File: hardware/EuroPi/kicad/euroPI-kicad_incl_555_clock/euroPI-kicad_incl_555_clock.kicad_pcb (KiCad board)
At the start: 2 copper layers, 121.9 x 128.5 mm, 108 parts, among them J1 Output 1 Jack, J10 Eurorack Power 2x8 16p, J11 Conn_01x13_Socket, J12 OLED 64x128, J13 USB_B_Micro, J14 Conn_01x03_Pin, J15 Conn_01x04_Pin, J16 Conn_02x04_Top_Bottom, J17 Conn_01x13_Pin, J18 Conn_01x04_Pin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

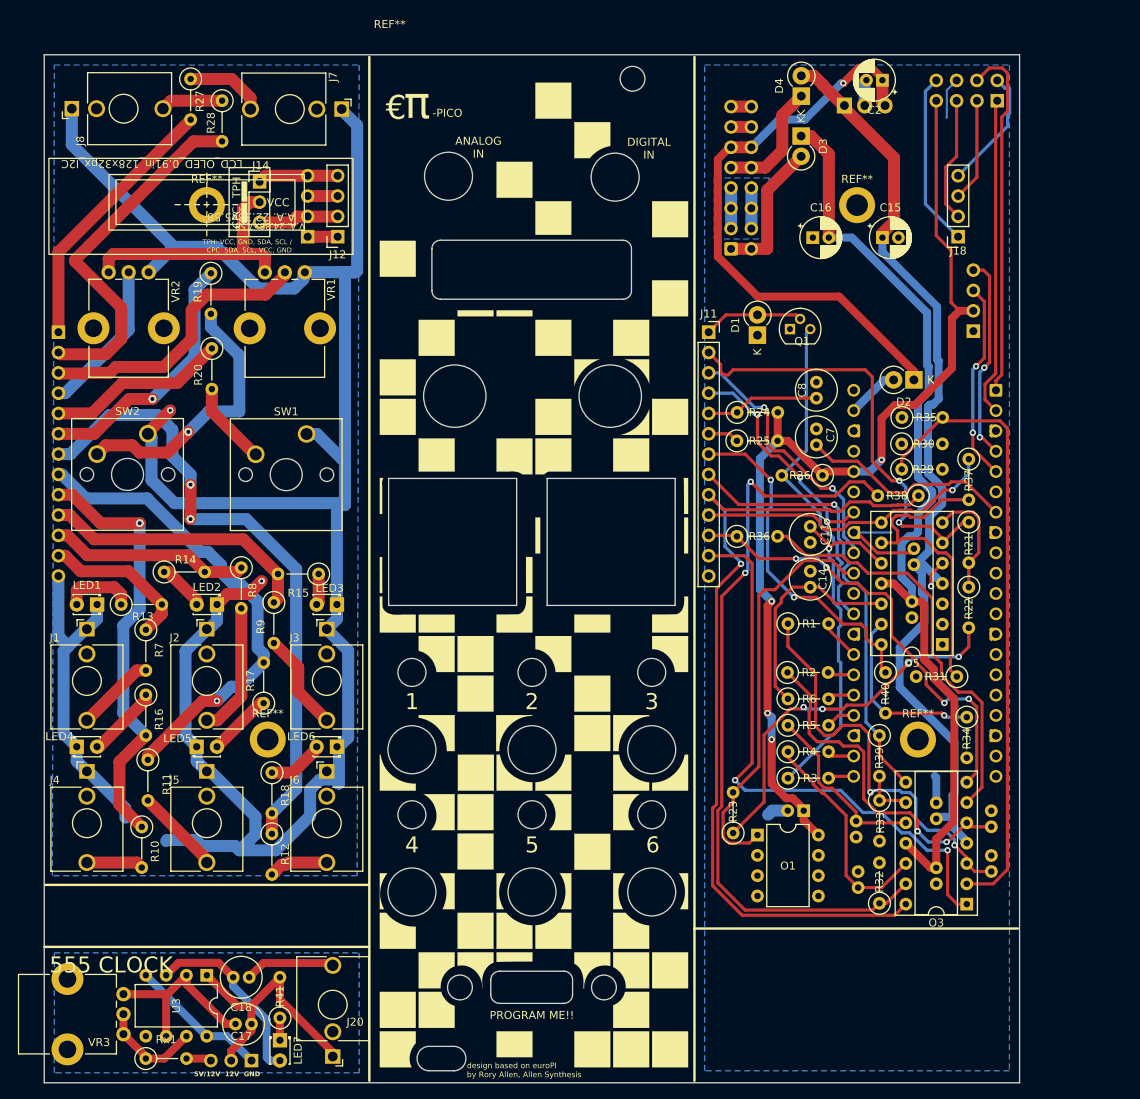
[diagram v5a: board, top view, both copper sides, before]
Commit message: incl standoffs to GND removed GND pin on headers
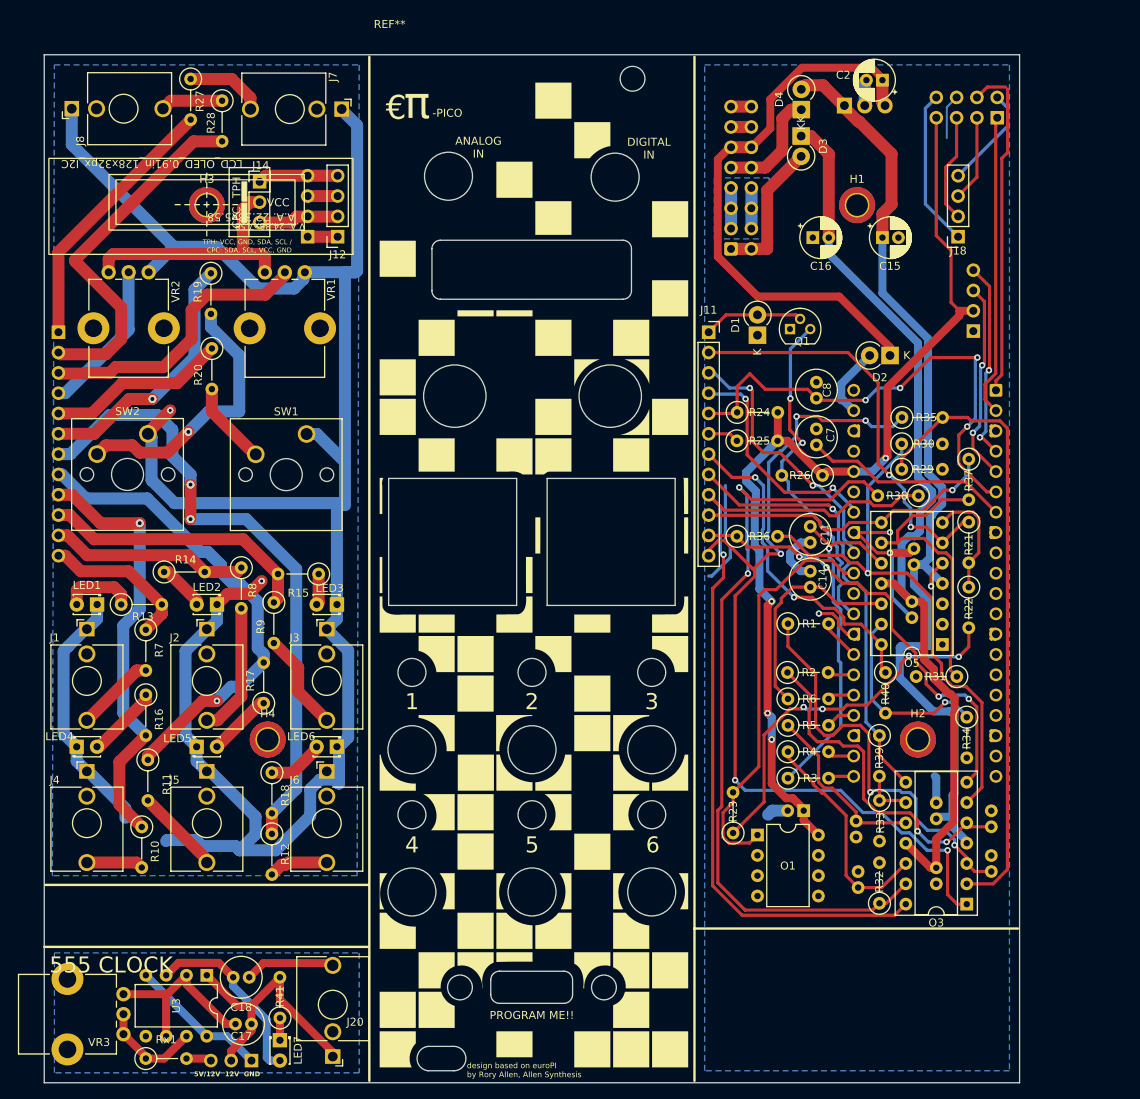
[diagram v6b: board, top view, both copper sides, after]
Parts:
- removed the REF** at (109.2, 111.0)
- removed the REF** at (101.6, 44.2)
- removed the REF** at (182.9, 44.2)
- removed the REF** at (190.5, 111.0)
- added H1: MountingHole_Pad, MountingHole:MountingHole_2.7mm_M2.5_ISO14580_Pad_TopBottom, F.Cu at (182.9, 44.2)
- added H2: MountingHole_Pad, MountingHole:MountingHole_2.7mm_M2.5_ISO14580_Pad_TopBottom, F.Cu at (190.5, 111.0)
- added H3: MountingHole_Pad, MountingHole:MountingHole_2.7mm_M2.5_ISO14580_Pad_TopBottom, F.Cu at (101.6, 44.2)
- added H4: MountingHole_Pad, MountingHole:MountingHole_2.7mm_M2.5_ISO14580_Pad_TopBottom, F.Cu at (109.2, 111.0)
- J11: value Conn_01x13_Socket -> Conn_01x12_Socket; footprint Connector_PinSocket_2.54mm:PinSocket_1x13_P2.54mm_Vertical -> Connector_PinSocket_2.54mm:PinSocket_1x12_P2.54mm_Vertical
- J17: value Conn_01x13_Pin -> Conn_01x12_Pin; footprint Connector_PinSocket_2.54mm:PinSocket_1x13_P2.54mm_Vertical -> Connector_PinHeader_2.54mm:PinHeader_1x12_P2.54mm_Vertical
- moved D2 4.27 mm to (187.0, 63.0)
- moved J16 2.12 mm to (200.4, 33.3)
- moved D4 1.69 mm to (175.9, 32.3)
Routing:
- net CS1: track 36.8 -> 84.0 mm, vias 0 -> 4
- net CJ1: track 91.9 -> 131.6 mm, vias 2 -> 5
- net I2C_GND: track 373.3 -> 399.3 mm, vias 3 -> 6
- net Net-(O3B--): track 52.4 -> 70.4 mm, vias 0 -> 1
- net CJA: track 100.3 -> 97.2 mm
- net TPH VCC / CPC SDA: track 25.7 -> 22.9 mm
- net ~: track 138.1 -> 140.9 mm
- net -12V: track 117.9 -> 115.3 mm
- net GP0: track 45.0 -> 42.4 mm
- net Net-(D2-K): track 6.58 -> 9.16 mm
- net +5V: track 76.4 -> 74.2 mm, vias 1 -> 0
- net TPH GND / CPC SCL: track 16.6 -> 14.4 mm
- net TPH SDA / CPC VCC: track 25.7 -> 23.6 mm
- net TPH SCL / CPC GND: track 25.5 -> 23.3 mm
- net GP1: track 39.9 -> 37.8 mm
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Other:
- board text added: "I2C"

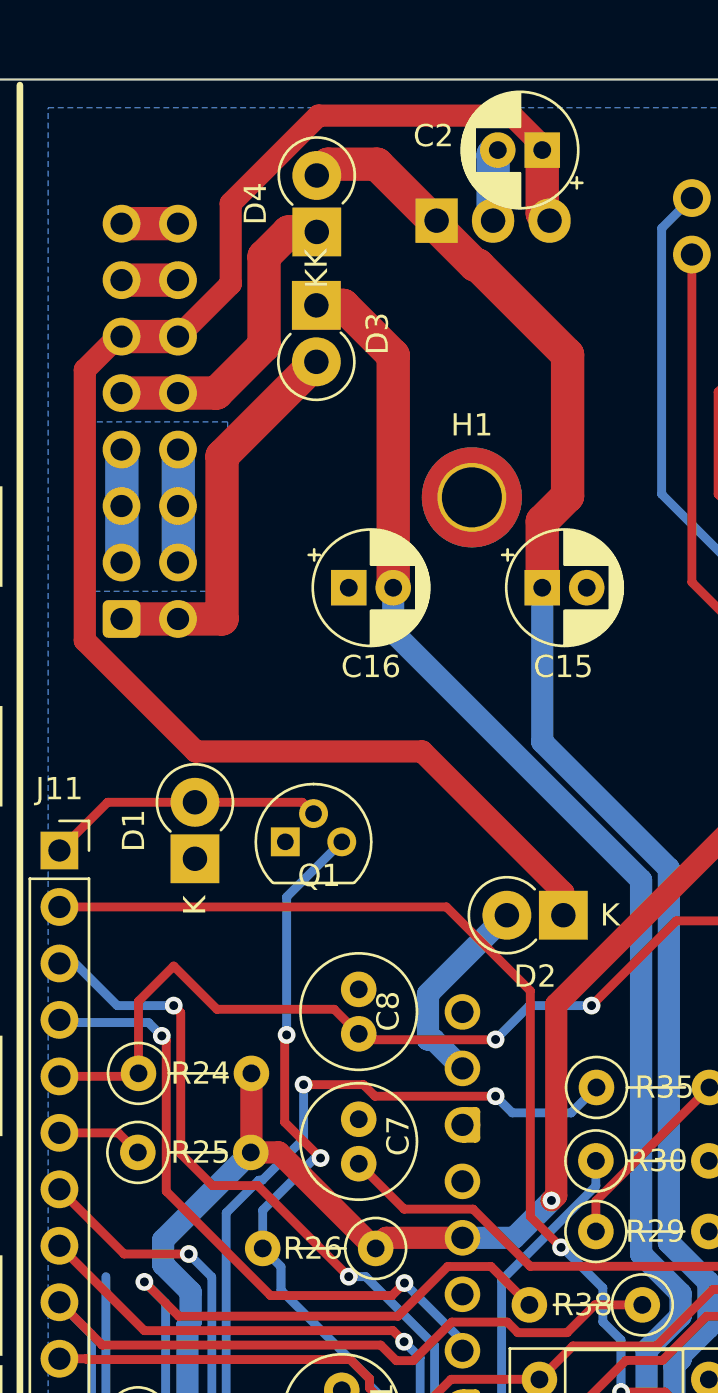
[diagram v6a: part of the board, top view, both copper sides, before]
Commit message: small fixes added missed net and text around eurorack conn
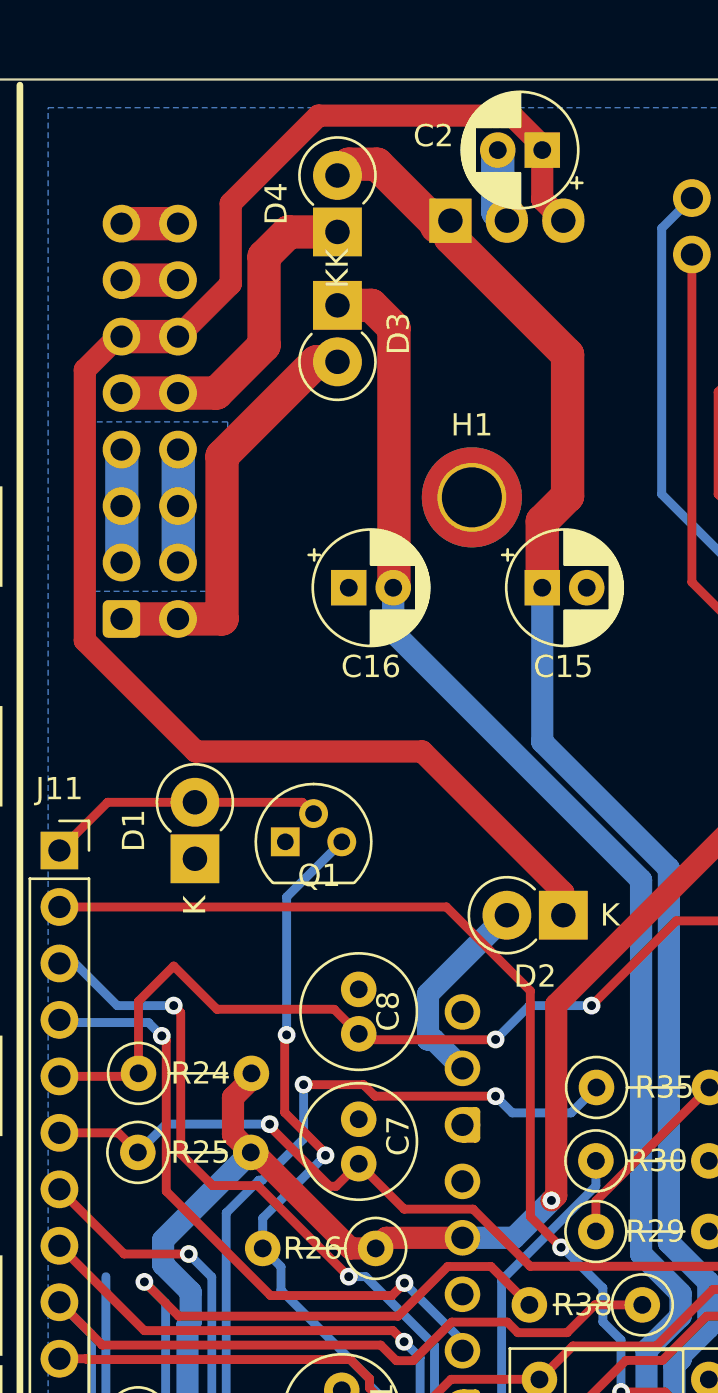
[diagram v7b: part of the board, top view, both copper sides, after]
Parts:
- moved D3 0.95 mm to (176.8, 35.6)
- moved D4 0.93 mm to (176.8, 32.3)
- moved U1 0.62 mm to (181.9, 31.8)
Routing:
- net CS2: track 62.1 -> 74.2 mm, vias 1 -> 2
- net ~: track 140.9 -> 139.8 mm
- net Net-(D3-K): track 17.9 -> 18.8 mm
- net Net-(D4-A): track 14.1 -> 15.0 mm
- net I2C_VCC: track 156.1 -> 156.8 mm
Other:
- board text added: "Gate CV +5V --- +12V GND GND GND -12V"

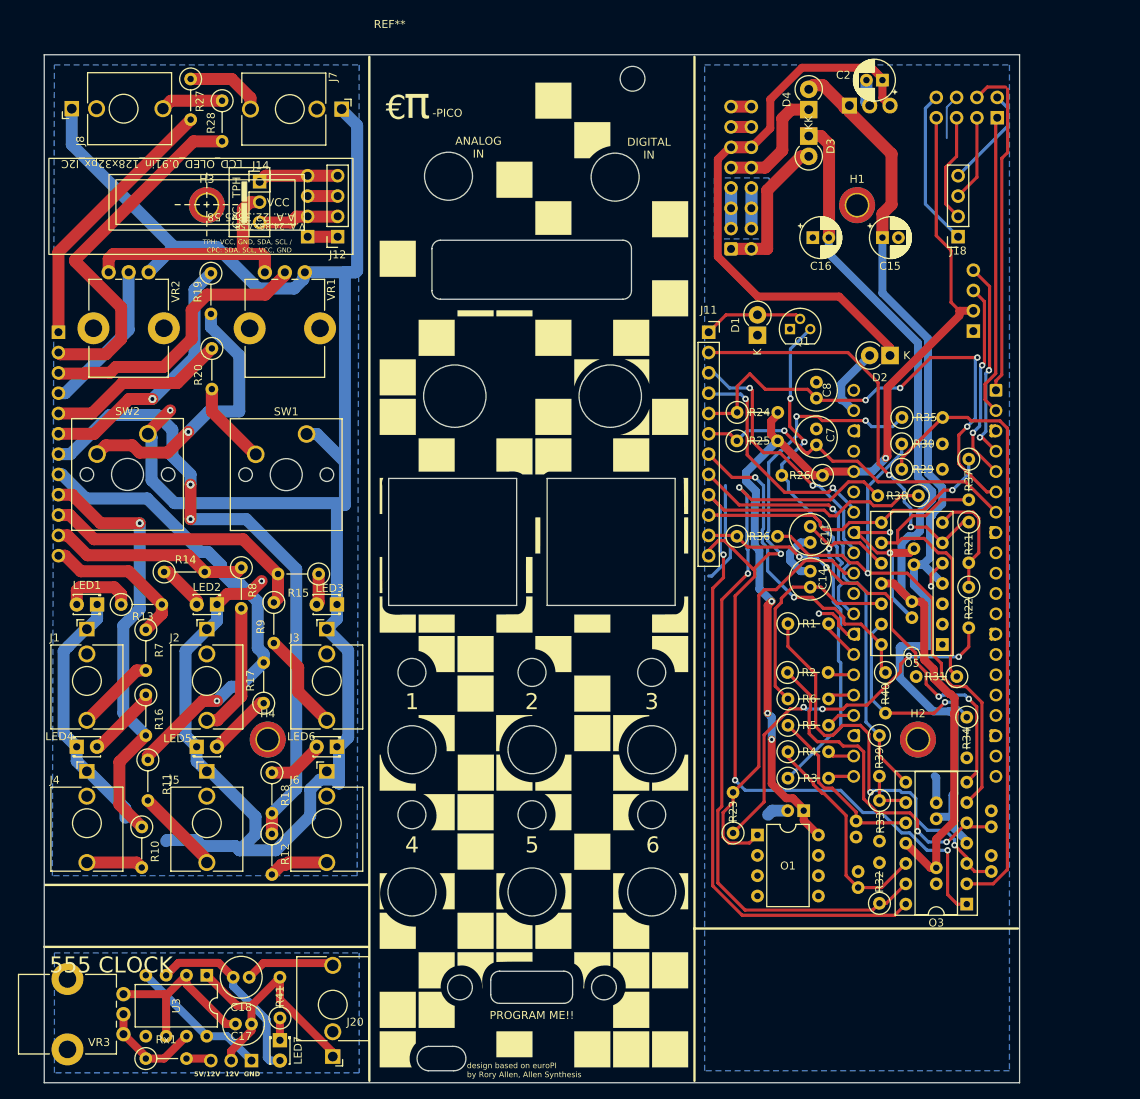
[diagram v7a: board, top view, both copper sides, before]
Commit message: misc improvements THT fixed grounds and misc clean up issue likely still wtih usb output SMT redid caps to be near to necessary fixed GND and misc things to make it easier to hand solder
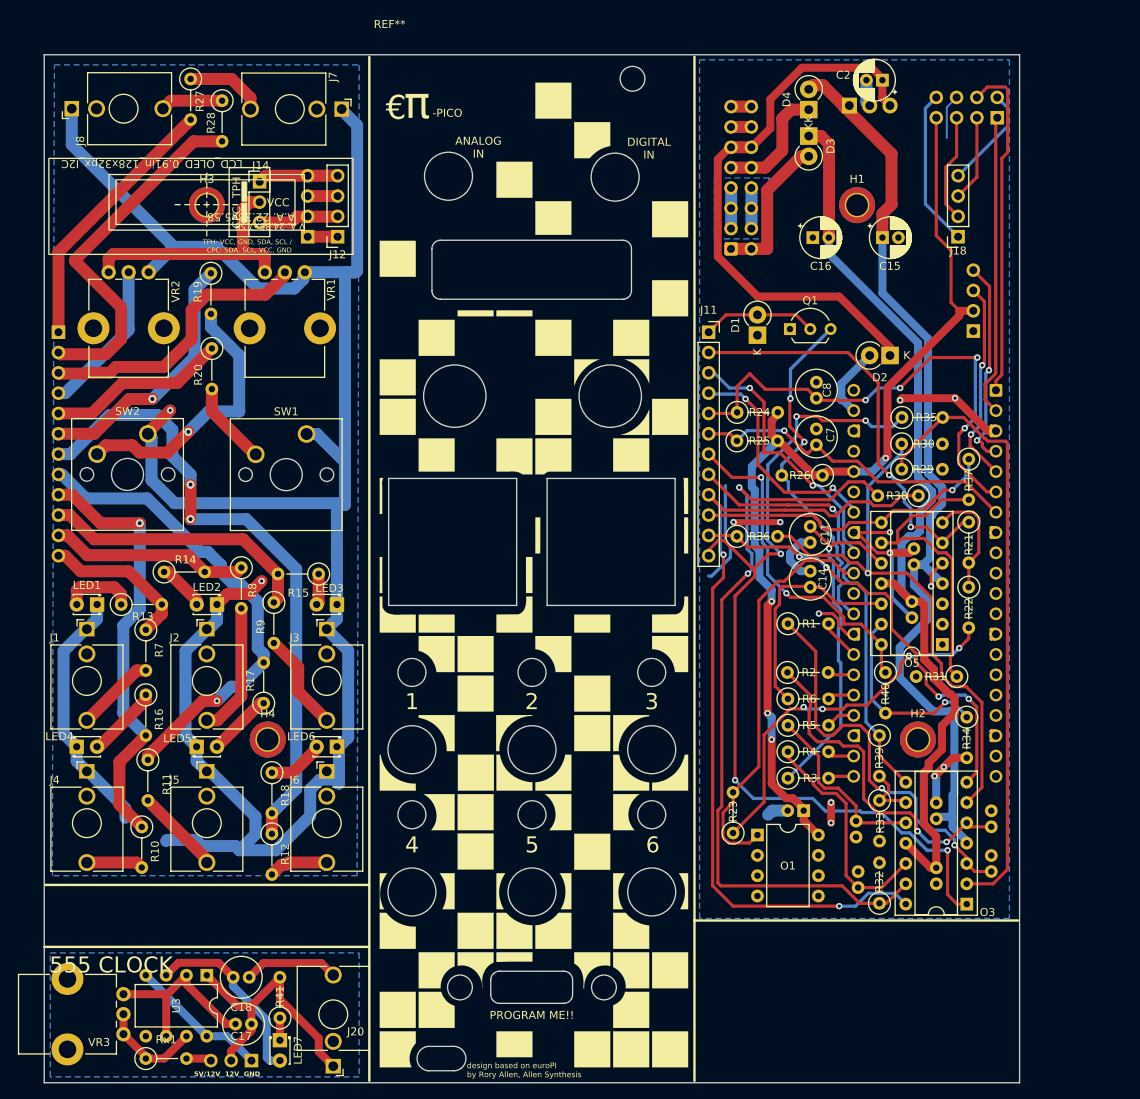
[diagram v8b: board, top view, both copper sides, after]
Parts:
- Q1: footprint Package_TO_SOT_THT:TO-92 -> Package_TO_SOT_THT:TO-92L_Inline_Wide
- moved J20 1.21 mm to (117.4, 151.8)
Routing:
- net I2C_GND: track 399.4 -> 425.2 mm, vias 6 -> 12
- net (no net): track 0.00 -> 2.54 mm, vias 0 -> 2
- net ~: track 139.8 -> 137.7 mm
- net CJD: track 46.0 -> 47.7 mm
- net -12V: track 115.1 -> 116.4 mm
- net Net-(O3A--): track 78.2 -> 77.2 mm
- net GP22: track 43.2 -> 44.2 mm
- net Net-(O3A-+): track 51.5 -> 50.5 mm
- net GP2: track 25.0 -> 25.9 mm
- net Net-(O3C--): track 6.45 -> 7.40 mm
- net Net-(O5D-+): track 27.5 -> 28.4 mm
- net Net-(O3D-+): track 27.9 -> 28.8 mm
- net I2C_VCC: track 156.8 -> 156.0 mm
- net Net-(O1A--): track 47.3 -> 46.7 mm
- net CJ6: track 120.9 -> 121.5 mm
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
